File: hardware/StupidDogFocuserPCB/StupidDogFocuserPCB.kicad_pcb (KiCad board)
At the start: 2 copper layers, 68.6 x 53.3 mm, 18 parts, among them M1 Stepper_Motor_bipolar, SW1 Rotary_Encoder_Switch, U1 DHT11, U2 SN74HC14N

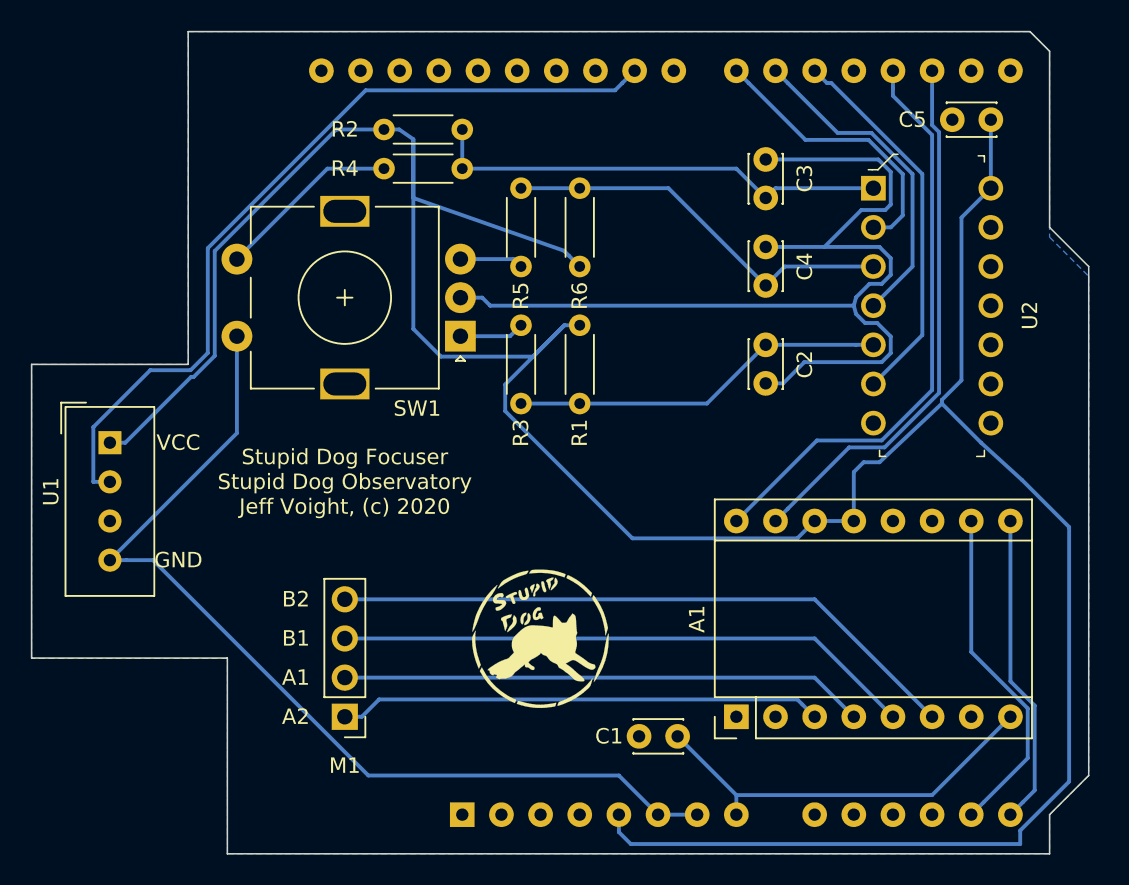
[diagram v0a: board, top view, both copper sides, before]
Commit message: Remap/pins (#14)
* Remapped kicad pins. Still need to map firmware.

* no connections added to unused pins.

* moved dht pin.

* moved pins in sketch. Added optimize interrupts flag. Changed error messages.
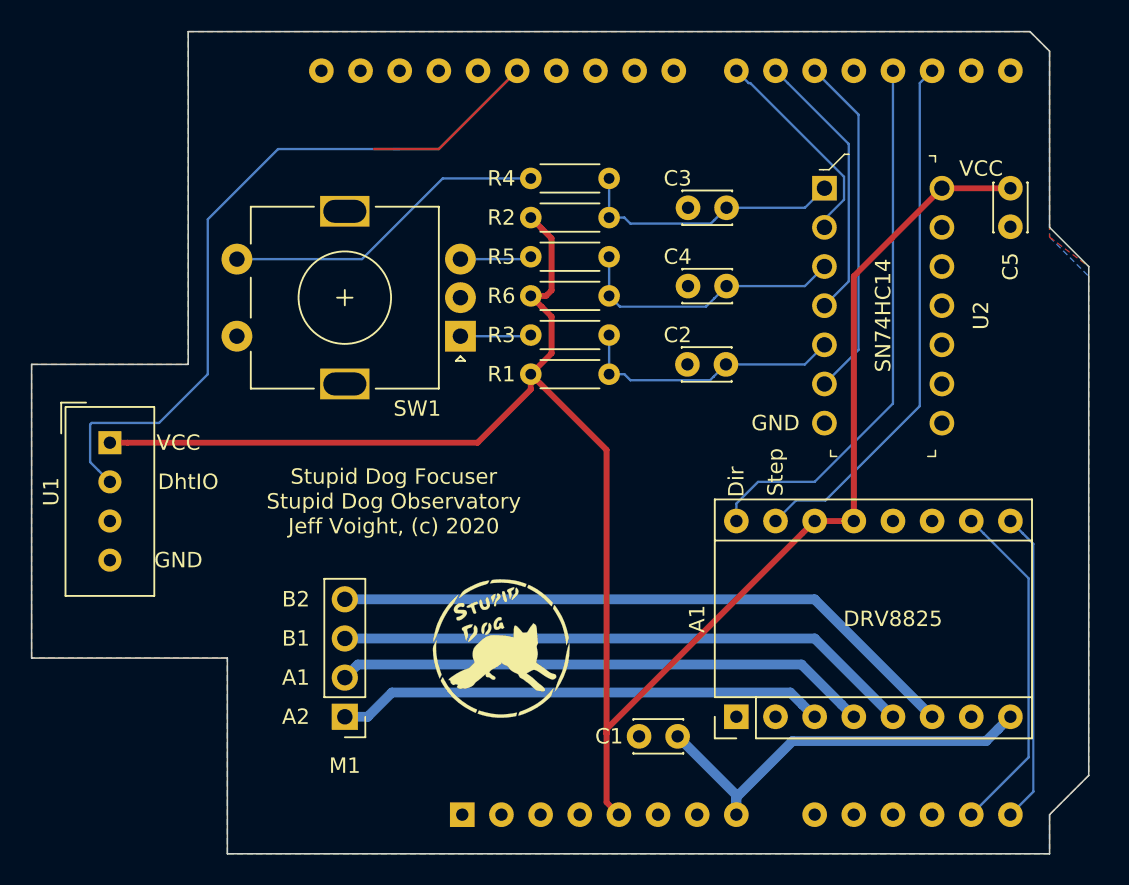
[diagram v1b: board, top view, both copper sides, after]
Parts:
- R1, R2, R3, R4, R5, R6: value R -> 1k
- moved R2 11.1 mm to (127.6, 69.2)
- moved R4 9.55 mm to (132.7, 66.7)
- moved R3 7.24 mm to (132.7, 76.8), turned to 180 degrees
- moved R6 7.24 mm to (132.7, 74.3), turned to 180 degrees
- moved C4 5.64 mm to (137.8, 73.7), turned to 0 degrees
- moved C5 4.62 mm to (158.8, 67.3), turned to 270 degrees
- moved R1 4.49 mm to (127.6, 79.4), turned to 0 degrees
- moved U2 3.18 mm to (146.7, 67.3)
- moved C2 2.88 mm to (140.3, 78.7), turned to 180 degrees
- moved G*** 2.62 mm to (125.7, 97.2)
- moved C3 2.62 mm to (140.3, 68.6), turned to 180 degrees
- moved R5 0.90 mm to (127.6, 71.8), turned to 0 degrees
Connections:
- A2 pad 24: DHT -> (no net)
- A2 pad 27: (no net) -> DHT
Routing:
- net GND: track 130.9 -> 0.00 mm
- net VCC: track 197.5 -> 124.0 mm
- net SW: track 30.3 -> 17.6 mm
- net Net-(R4-Pad2): track 12.0 -> 21.2 mm
- net ENC_B: track 26.0 -> 17.9 mm
- net ENC_A: track 24.4 -> 17.6 mm
- net DHT: track 53.3 -> 59.1 mm
- net SW_A: track 18.5 -> 13.6 mm
- net ENCB_A: track 21.3 -> 17.9 mm
- net Dir: track 38.0 -> 35.6 mm
- net ENCA_A: track 24.7 -> 22.4 mm
- net VDD: track 26.5 -> 27.7 mm
- net A1: track 34.1 -> 34.8 mm
- net Step: track 35.1 -> 34.5 mm
- net Net-(R5-Pad1): track 4.13 -> 4.63 mm
- added copper zone on F.Cu, net GND
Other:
- net class 12V added: clearance 0.4572, trace_width 0.635, via_dia 0.762, via_drill 0.3302
- net class 5V added: clearance 0.3048, trace_width 0.381, via_dia 0.6858, via_drill 0.3302
- net class Default: clearance 0.2 -> 0.1524; trace_width 0.25 -> 0.1524; via_dia 0.8 -> 0.6858; via_drill 0.4 -> 0.3302
- rule pad_to_mask_clearance: 0.051 -> 0.0508
- rule solder_mask_min_width: 0.25 -> 0.1016
- rule trace_clearance: 0.2 -> 0.1524
- rule trace_min: 0.2 -> 0.1524
- rule via_min_drill: 0.3 -> 0.254
- rule via_min_size: 0.4 -> 0.508
- board text added: "DRV8825"
- board text added: "DhtIO"
- board text added: "Dir"
- board text added: "SN74HC14"
- board text added: "Step"

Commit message: Indi/clearout (#16)
* gitignore

* Deleted Backlash, speed controls, and switches.

* Serial Connection. Updated sendCommand and readResponse to handle tty.

* erant trace removed

* thicker traces

* gitignore

* Deleted Backlash, speed controls, and switches.

* Serial Connection. Updated sendCommand and readResponse to handle tty.

* erant trace removed

* thicker traces

Co-authored-by: Jeff Voight <jeff.voight@coveros.com>
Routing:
- net DHT: track 59.1 -> 49.0 mm
- net ~Enable: track 20.3 -> 21.2 mm
- net ENCA_A: track 22.4 -> 23.2 mm
- net SW: track 17.6 -> 18.4 mm
- net HalfStep: track 22.1 -> 22.7 mm

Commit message: Hardware/cleanup (#22)
* added m1 and m2

* gerbers
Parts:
- moved G*** 29.9 mm to (155.6, 99.1)
- moved A1 18.5 mm to (122.6, 103.5)
- moved C1 10.2 mm to (144.8, 101.6), turned to 270 degrees
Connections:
- net HalfStep renamed M0
- A1 pad 11: (no net) -> M1
- A1 pad 12: (no net) -> M2
- A2 pad 11: (no net) -> M2
- A2 pad 12: (no net) -> M1
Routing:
- net M2: track 0.00 -> 26.5 mm
- net M1: track 0.00 -> 25.5 mm
- net A2: track 31.8 -> 12.9 mm
- net VDD: track 27.7 -> 9.40 mm
- net A1: track 34.8 -> 16.4 mm
- net Dir: track 35.6 -> 53.2 mm
- net B1: track 37.7 -> 20.0 mm
- net B2: track 41.3 -> 23.6 mm
- net Step: track 34.6 -> 52.2 mm
- net VCC: track 124.0 -> 139.5 mm
- net ~Enable: track 21.2 -> 25.5 mm
- net M0: track 22.7 -> 25.5 mm
- net SW_A: track 13.6 -> 14.3 mm

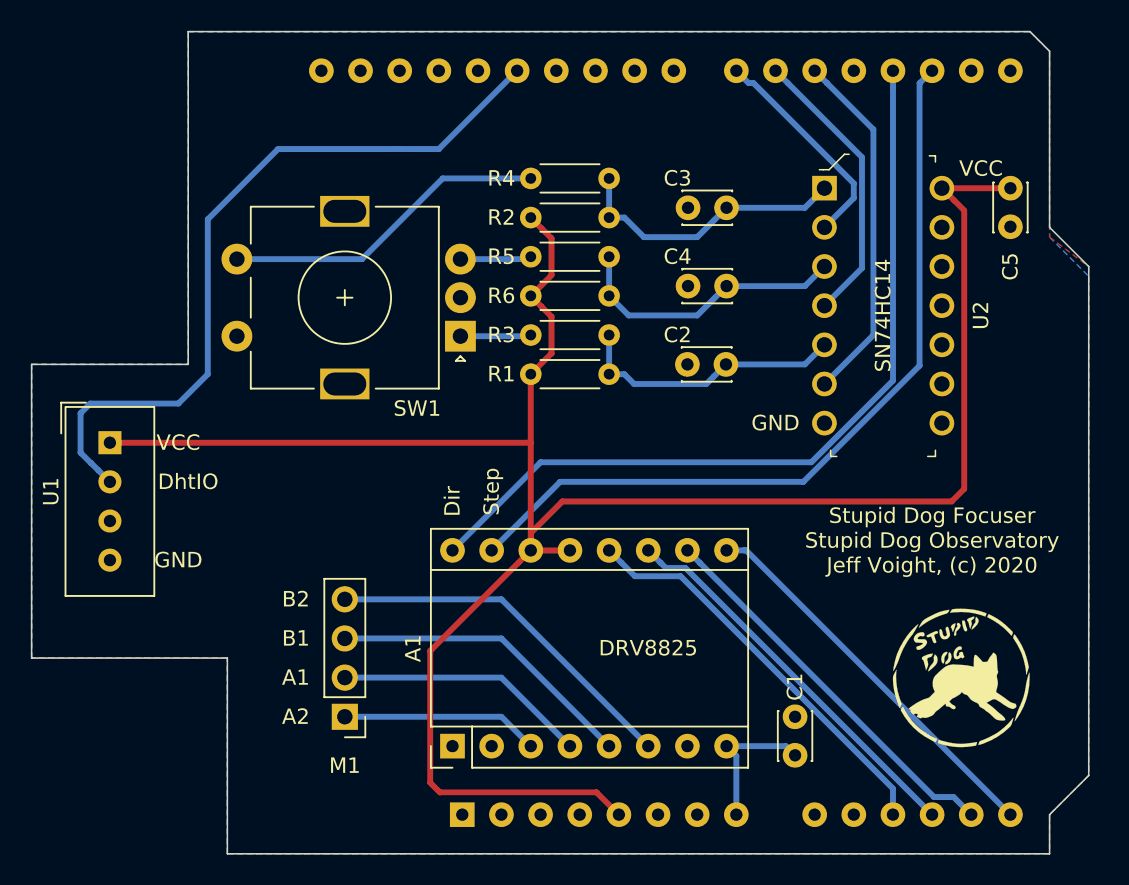
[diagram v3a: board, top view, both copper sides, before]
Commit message: Hardware/bugs (#26)
* ASCOM6 Template

* ASCOM commands ported in from firmware

* remove readme.htm. Will replace with Readme.md when I get around to it.

* Updated schematic. Added limit switch. Moved encoder to the right and the stepper to the left. Adjusted resistor and capacitor sizes. Added screw terminals. Moved DHT11 to where it can bend out.

* thicker traces for the home gamer. Cleanup bends. Moved test points around.

* regenerate gerbers

* pcb

Co-authored-by: Jeff Voight <jeff.voight@gmail.com>
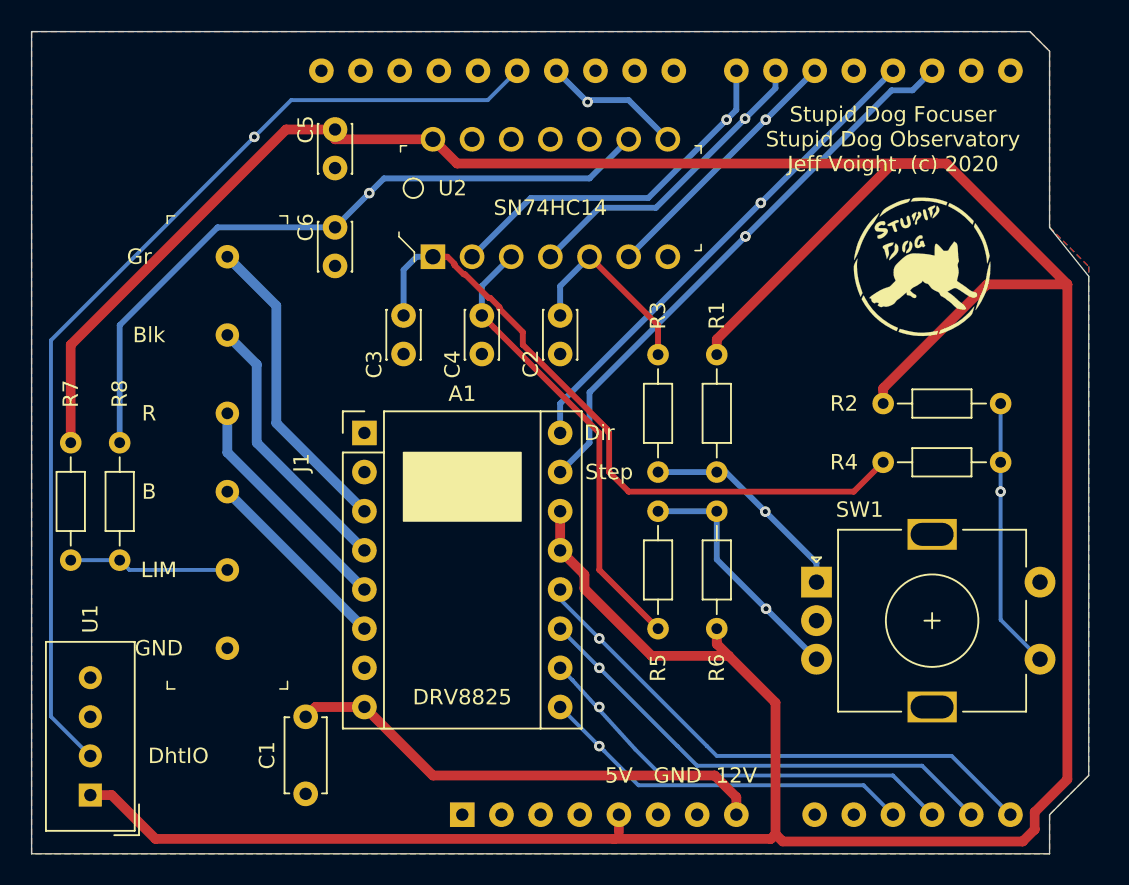
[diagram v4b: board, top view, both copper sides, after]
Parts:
- removed M1: Stepper_Motor_bipolar, Connector_PinHeader_2.54mm:PinHeader_1x04_P2.54mm_Vertical
- added C6: 4.7uF, Capacitor_THT:C_Disc_D3.0mm_W2.0mm_P2.50mm, F.Cu at (114.9, 69.8)
- added J1: OSTTC062162, digikey-footprints:Term_Block_1x6_P5.08mm, F.Cu at (108.0, 71.8)
- added R7: 1k, Resistor_THT:R_Axial_DIN0204_L3.6mm_D1.6mm_P7.62mm_Horizontal, F.Cu at (97.8, 83.8)
- added R8: 1k, Resistor_THT:R_Axial_DIN0204_L3.6mm_D1.6mm_P7.62mm_Horizontal, F.Cu at (101.0, 83.8)
- C1: footprint Capacitor_THT:C_Disc_D3.0mm_W2.0mm_P2.50mm -> Capacitor_THT:C_Disc_D4.7mm_W2.5mm_P5.00mm
- R1, R2, R3, R4, R5, R6: footprint Resistor_THT:R_Axial_DIN0204_L3.6mm_D1.6mm_P5.08mm_Horizontal -> Resistor_THT:R_Axial_DIN0204_L3.6mm_D1.6mm_P7.62mm_Horizontal
- moved C5 44.0 mm to (114.9, 63.5)
- moved C1 32.1 mm to (113.0, 106.6), turned to 90 degrees
- moved SW1 28.1 mm to (146.2, 92.9), turned to 0 degrees
- moved G1 26.8 mm to (153.0, 72.4)
- moved R2 25.8 mm to (150.5, 81.3)
- moved U2 25.8 mm to (121.3, 71.8), turned to 90 degrees
- moved R4 25.6 mm to (150.5, 85.1), turned to 0 degrees
- moved U1 22.9 mm to (99.1, 106.7), turned to 180 degrees
- moved C3 22.1 mm to (119.4, 75.6), turned to 270 degrees
- moved A1 21.1 mm to (116.8, 83.2), turned to 0 degrees
- moved R5 18.5 mm to (135.9, 88.3), turned to 270 degrees
- moved R6 15.6 mm to (139.7, 88.3), turned to 270 degrees
- moved C4 14.1 mm to (124.5, 78.1), turned to 90 degrees
- moved R1 12.1 mm to (139.7, 78.1), turned to 270 degrees
- moved C2 11.2 mm to (129.5, 75.6), turned to 270 degrees
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- renumbered G*** to G1
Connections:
- A1 pad 3: A2 -> G
- A1 pad 4: A1 -> BLK
- A1 pad 5: B1 -> R
- A1 pad 6: B2 -> BL
- A2 pad 11: M2 -> ~Enable
- A2 pad 12: M1 -> M0
- A2 pad 13: M0 -> M1
- A2 pad 14: ~Enable -> M2
- A2 pad 20: ENCA_A -> ENCA
- A2 pad 21: ENCB_A -> ENCB
- A2 pad 22: SW_A -> SW
- A2 pad 26: (no net) -> LIM
- C2 pad 1: ENC_A -> ENCA_A
- C3 pad 1: SW -> SW_A
- C4 pad 2: ENC_B -> ENCB_A
- R1 pad 2: ENC_A -> Net-(R1-Pad2)
- R2 pad 2: SW -> Net-(R2-Pad2)
- R3 pad 1: ENC_A -> ENCA_A
- R3 pad 2: Net-(R3-Pad2) -> Net-(R1-Pad2)
- R4 pad 1: SW -> SW_A
- R4 pad 2: Net-(R4-Pad2) -> Net-(R2-Pad2)
- R5 pad 2: ENC_B -> ENCB_A
- R6 pad 1: ENC_B -> Net-(R5-Pad1)
- SW1 pad A: Net-(R3-Pad2) -> Net-(R1-Pad2)
- SW1 pad S1: Net-(R4-Pad2) -> Net-(R2-Pad2)
- U2 pad 1: SW -> SW_A
- U2 pad 2: SW_A -> SW
- U2 pad 3: ENC_B -> ENCB_A
- U2 pad 4: ENCB_A -> ENCB
- U2 pad 5: ENC_A -> ENCA_A
- U2 pad 6: ENCA_A -> ENCA
- U2 pad 8: (no net) -> LIM
- U2 pad 9: (no net) -> LIM_A
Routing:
- net VCC: track 139.5 -> 251.0 mm
- net LIM_A: track 0.00 -> 45.6 mm, vias 0 -> 1
- net SW_A: track 14.3 -> 43.7 mm
- net B2: track 23.6 -> 0.00 mm
- net VDD: track 9.40 -> 31.8 mm
- net Net-(R4-Pad2): track 21.2 -> 0.00 mm
- net Dir: track 53.2 -> 32.4 mm, vias 0 -> 1
- net ENCB: track 0.00 -> 20.3 mm, vias 0 -> 1
- net G: track 0.00 -> 20.2 mm
- net B1: track 20.0 -> 0.00 mm
- net ENC_B: track 18.4 -> 0.00 mm
- net ENC_A: track 17.8 -> 0.00 mm
- net BLK: track 0.00 -> 17.7 mm
- net Net-(R2-Pad2): track 0.00 -> 17.6 mm, vias 0 -> 1
- net ENCA: track 0.00 -> 17.1 mm, vias 0 -> 1
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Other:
- outline, holes or cut-outs redrawn
- board text added: "12V"
- board text added: "5V"
- board text added: "B"
- board text added: "Blk"
- board text added: "Gr"
- board text added: "LIM"
- board text added: "R"
- board text removed: "A1"
- board text removed: "A2"
- board text removed: "B1"
- board text removed: "B2"
- board text removed: "VCC"

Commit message: Feature/bompcbpads (#31)
* bill of materials

* added ground clip pad. Updated capacitor sizes. Regenerated gerbers.

Co-authored-by: Jeff Voight <jeff.voight@gmail.com>
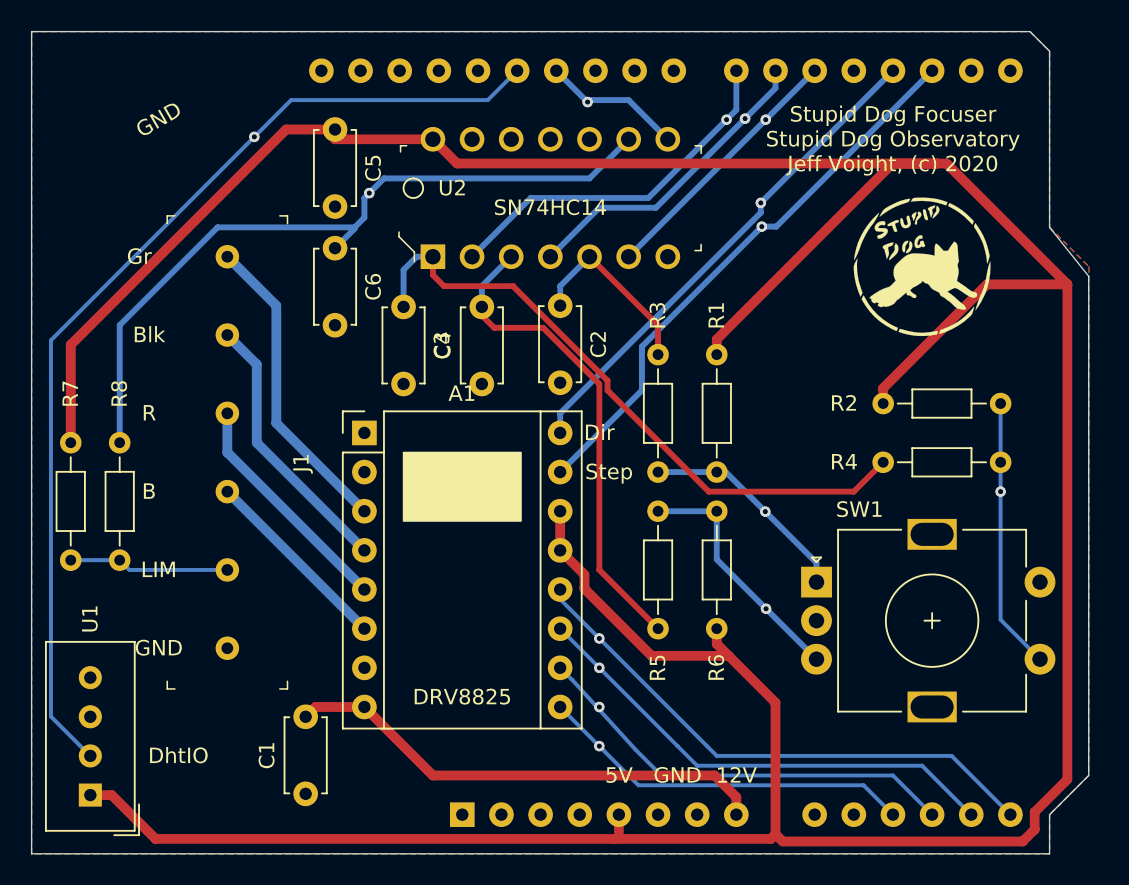
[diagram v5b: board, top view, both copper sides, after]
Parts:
- C2, C3, C4, C5, C6: footprint Capacitor_THT:C_Disc_D3.0mm_W2.0mm_P2.50mm -> Capacitor_THT:C_Disc_D4.7mm_W2.5mm_P5.00mm
- moved C4 1.95 mm to (124.5, 80.0)
- moved C6 1.35 mm to (114.9, 71.2)
- moved C2 0.63 mm to (129.5, 74.9)
- moved C3 0.55 mm to (119.4, 75.0)
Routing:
- net LIM_A: track 45.6 -> 48.3 mm
- net ENCB_A: track 29.7 -> 31.5 mm
- net SW_A: track 43.7 -> 42.6 mm
